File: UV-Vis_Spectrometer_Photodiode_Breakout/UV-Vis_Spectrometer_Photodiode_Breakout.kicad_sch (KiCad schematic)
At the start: 0 parts

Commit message: UV-Vis Photometer Circuit Diagram
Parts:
- added C1, C5, C6: C, symbol Device:C
- added C7, C9: 0.1uF, symbol Device:C
- added C8: 10uF, symbol Device:C
- added D1: BPW21R, OptoDevice:Kodenshi_LG206D, symbol Device:D_Photo
- added R1: R_US, Package_DIP:DIP-8_W7.62mm, symbol Device:R_US
- added R4: 1k, symbol Device:R_US
- added U1: TLV8811DBVR, Package_TO_SOT_SMD:SOT-353_SC-70-5, symbol Amplifier_Operational:TLV172IDCK
- added U3: LTC2451, Package_DFN_QFN:DFN-8-1EP_2x3mm_P0.5mm_EP0.61x2.2mm, symbol Analog_ADC:LTC2451xDDB
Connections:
- new net: C1.1, D1.1 (K), R1.1, U1.3 (-)
- new net: C1.2, R1.2, U1.4
- new net: C9.1, R4.2, U3.6 (IN)
- new net +3.3V: C7.1, C8.1, U3.3 (REF+), U3.4 (VCC)
- new net +3V3: C5.1, C6.1, U1.5 (V+)
- new net Clock: U3.7 (SCL)
- new net Data: U3.8 (SDA)
- new net GND: C5.2, C6.2, C7.2, C8.2, C9.2, D1.2 (A), U1.1 (+), U1.2 (V-), U3.1 (GND), U3.2 (REF-), U3.5 (GND), U3.9 (GND)
- new net Out_TIA: R4.1
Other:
- added sheet Power (untitled.kicad_sch)

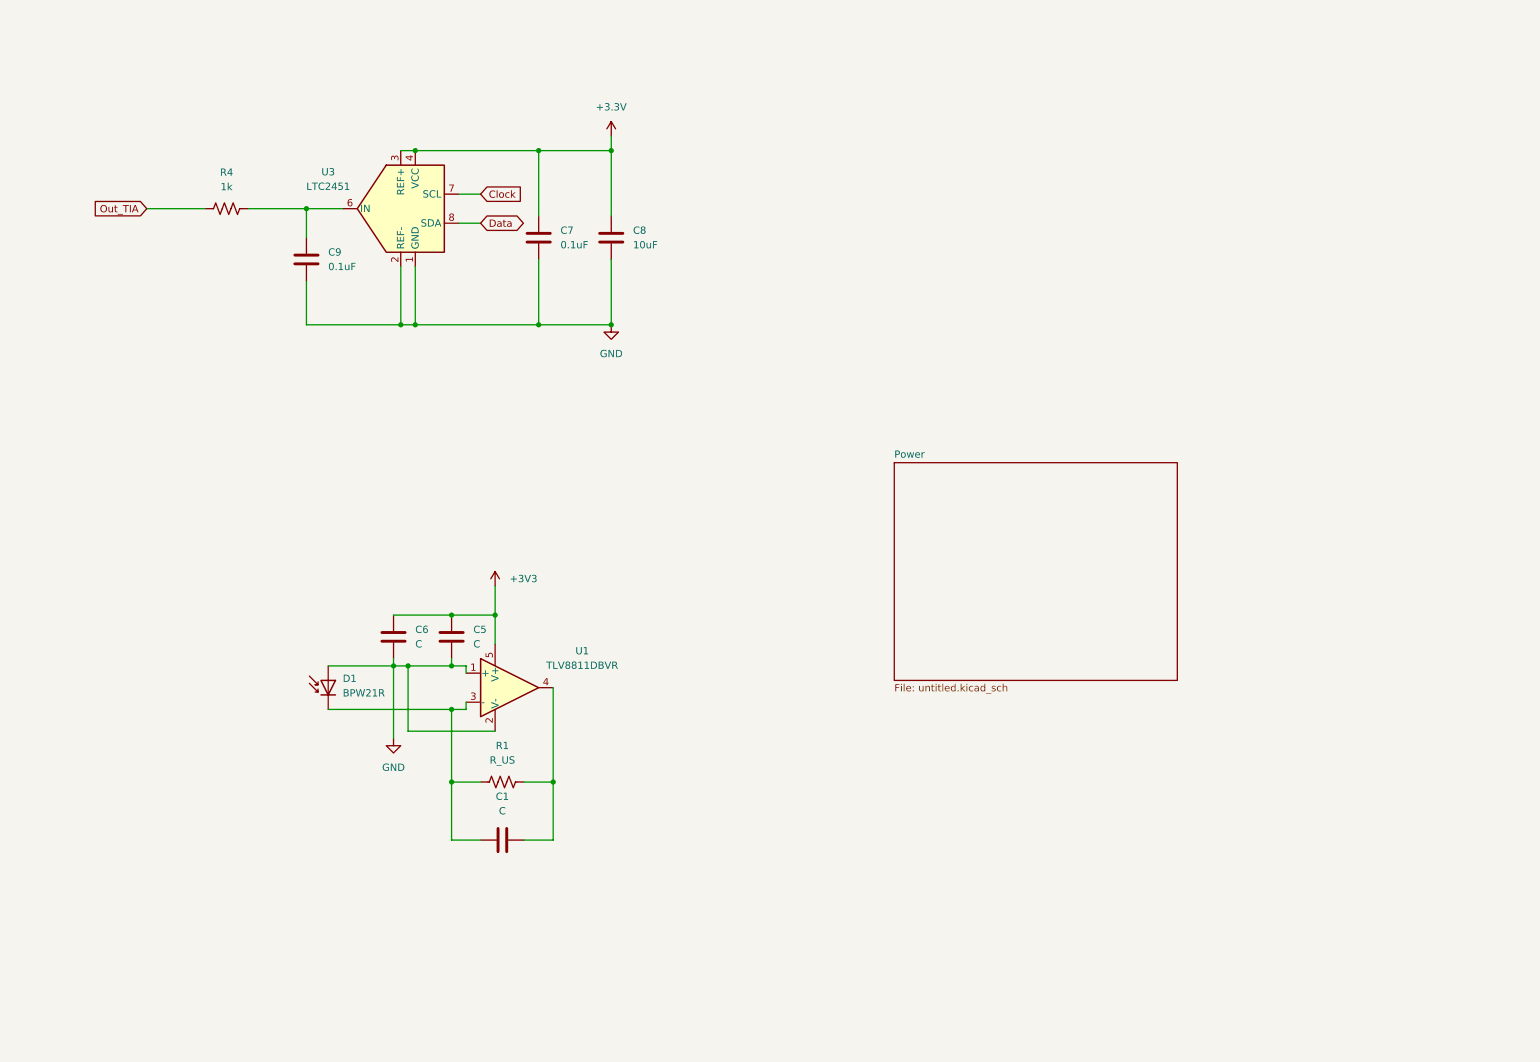
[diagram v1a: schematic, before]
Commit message: added reed switches, res values needed
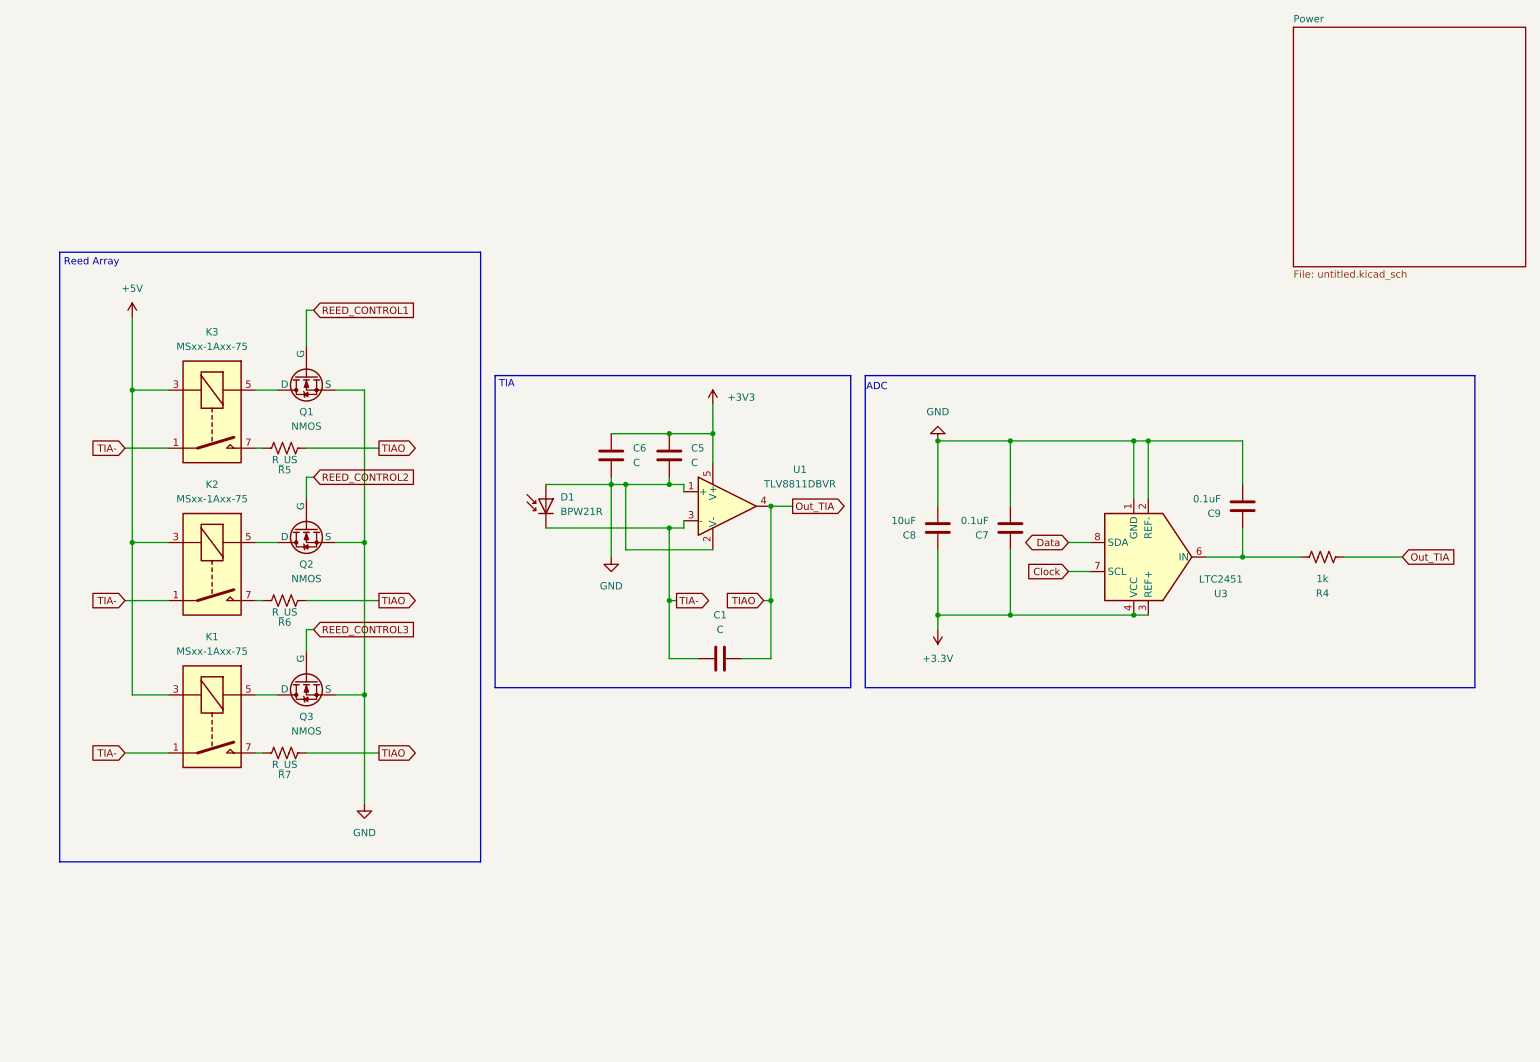
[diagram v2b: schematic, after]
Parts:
- removed R1: R_US, Package_DIP:DIP-8_W7.62mm, symbol Device:R_US
- added K1, K2, K3: MSxx-1Axx-75, Relay_THT:Relay_SPST_StandexMeder_MS_Form1AB, symbol Relay:MSxx-1Axx-75
- added Q1, Q2, Q3: NMOS, Package_DFN_QFN:Nordic_AQFN-94-1EP_7x7mm_P0.4mm, symbol Simulation_SPICE:NMOS
- added R5, R6, R7: R_US, Package_DIP:DIP-8_W7.62mm, symbol Device:R_US
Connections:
- net GND: now also Q1.3 (S), Q2.3 (S), Q3.3 (S)
- net Out_TIA: now also C1.2, U1.4, R5.2, R6.2, R7.2
- net TIA-: now reaches C1.1, D1.1 (K), U1.3 (-)
- net TIA-: now also K1.1, K2.1, K3.1
- new net: K2.7, R6.1
- new net: K3.5, Q1.1 (D)
- new net: K3.7, R5.1
- new net: K1.5, Q3.1 (D)
- new net: K2.5, Q2.1 (D)
- new net: K1.7, R7.1
- new net +5V: K1.3, K2.3, K3.3
- new net REED_CONTROL1: Q1.2 (G)
- new net REED_CONTROL2: Q2.2 (G)
- new net REED_CONTROL3: Q3.2 (G)
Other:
- note added: "ADC"
- note added: "Reed Array"
- note added: "TIA"
- moved on the sheet: C1, C5, C6, C7, C8, C9, D1, R4, U1, U3

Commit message: Added Connectors and Resistance values for the TIA
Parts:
- added J1: Conn_01x05, Package_DFN_QFN:QFN-20-1EP_5x5mm_P0.65mm_EP3.35x3.35mm, symbol Connector_Generic:Conn_01x05
- added J2: Conn_01x02, Package_DFN_QFN:QFN-20-1EP_5x5mm_P0.65mm_EP3.35x3.35mm, symbol Connector_Generic:Conn_01x02
- added J3: Conn_01x02, symbol Connector_Generic:Conn_01x02
- C1: value C -> 46pF
- C5: value C -> 10uF
- C6: value C -> 0.1uF
- R5: value R_US -> 5.1k
- R6: value R_US -> 8.2k
- R7: value R_US -> 16k
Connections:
- net +3V3: now also J3.1 (Pin_1)
- net +5V: now also J1.1 (Pin_1)
- net Clock: now also J2.2 (Pin_2)
- net Data: now also J2.1 (Pin_1)
- net GND: now also J1.2 (Pin_2), J3.2 (Pin_2)
- net REED_CONTROL1: now also J1.3 (Pin_3)
- net REED_CONTROL2: now also J1.4 (Pin_4)
- net REED_CONTROL3: now also J1.5 (Pin_5)

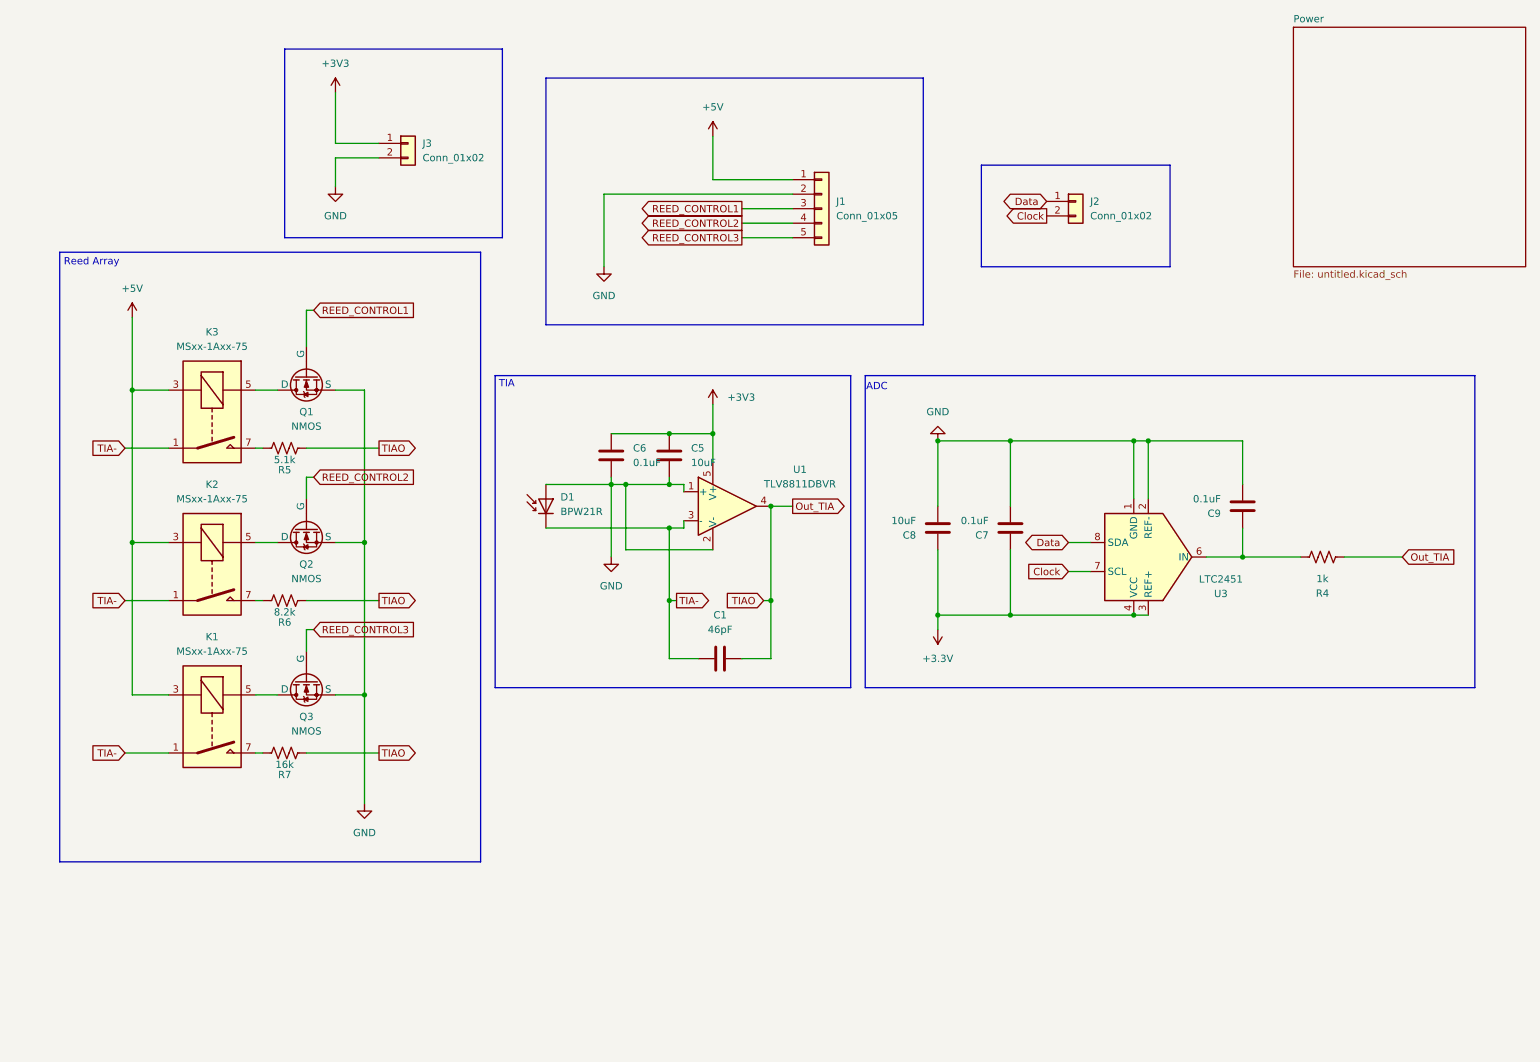
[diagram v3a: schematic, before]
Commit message: Cleaned up op amp circuit. Added Vref. Made reed relay symbol.
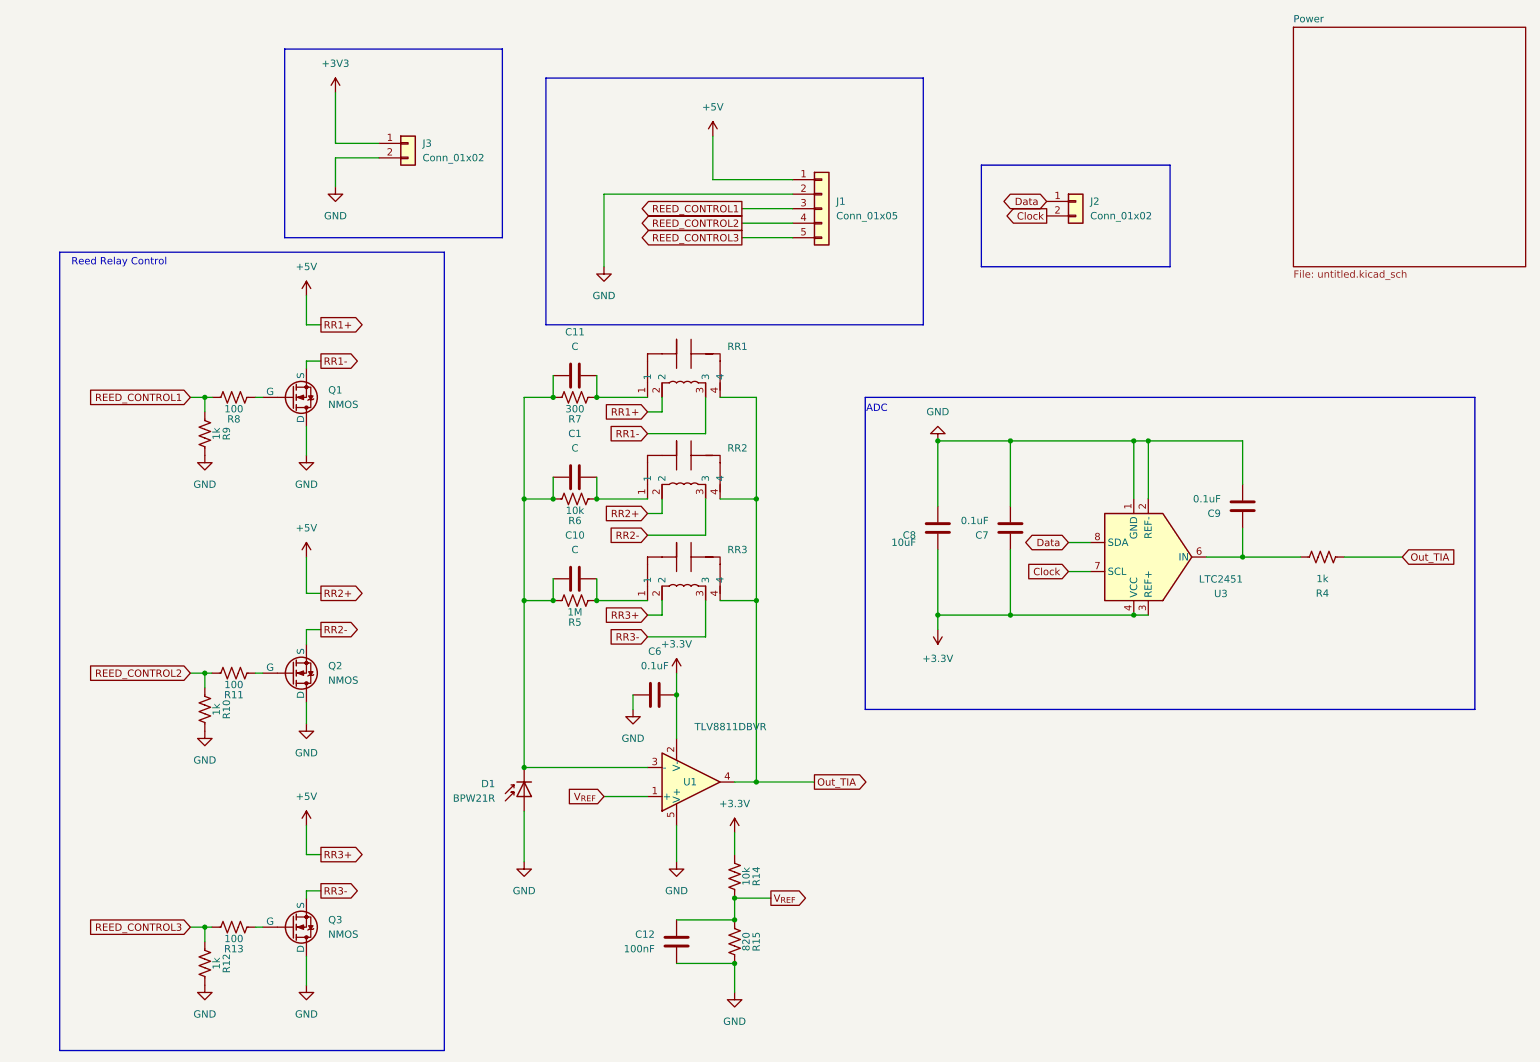
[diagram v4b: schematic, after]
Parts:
- removed C5: 10uF, symbol Device:C
- removed K1, K2, K3: MSxx-1Axx-75, Relay_THT:Relay_SPST_StandexMeder_MS_Form1AB, symbol Relay:MSxx-1Axx-75
- added C10, C11: C, symbol Device:C
- added C12: 100nF, symbol Device:C
- added R10, R12, R9: 1k, Package_DIP:DIP-8_W7.62mm, symbol Device:R_US
- added R11, R13, R8: 100, Package_DIP:DIP-8_W7.62mm, symbol Device:R_US
- added R14: 10k, Package_DIP:DIP-8_W7.62mm, symbol Device:R_US
- added R15: 820, Package_DIP:DIP-8_W7.62mm, symbol Device:R_US
- added RR1, RR2, RR3: (no value), symbol UV-Vis_Symbol_Library:9007-05-00
- C1: value 46pF -> C
- R5: value 5.1k -> 1M
- R6: value 8.2k -> 10k
- R7: value 16k -> 300
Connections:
- net TIA- is gone; now on an unnamed net: C1.1, D1.1 (K), U1.3 (-)
- net +3.3V: now also C6.2, U1.2 (V-), R14.2
- net +3V3: no longer C6.1, U1.5 (V+)
- net +5V: now also RR1.2, RR2.2, RR3.2
- net GND: now also C6.1, Q1.1 (D), Q2.1 (D), Q3.1 (D), U1.5 (V+), C12.2, R10.1, R12.1, R15.1, R9.1; no longer C6.2, Q1.3 (S), Q2.3 (S), Q3.3 (S), U1.1 (+), U1.2 (V-)
- net Out_TIA: now also RR1.4, RR2.4, RR3.4; no longer C1.2, R5.2, R6.2, R7.2
- net REED_CONTROL1: now also R8.1, R9.2; no longer Q1.2 (G)
- net REED_CONTROL2: now also R10.2, R11.1; no longer Q2.2 (G)
- net REED_CONTROL3: now also R12.2, R13.1; no longer Q3.2 (G)
- net at R6.1: now also R5.1, R7.1, C10.1, C11.1
- new net: C1.2, R6.2, RR2.1
- new net: Q3.2 (G), R13.2
- new net: Q2.2 (G), R11.2
- new net: Q1.2 (G), R8.2
- new net: C11.2, R7.2, RR1.1
- new net: C10.2, R5.2, RR3.1
- new net RR1-: Q1.3 (S), RR1.3
- new net RR2-: Q2.3 (S), RR2.3
- new net RR3-: Q3.3 (S), RR3.3
- new net V_{REF}: C12.1, R14.1, R15.2, U1.1 (+)
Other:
- note added: "Reed Relay Control"
- note removed: "Reed Array"
- note removed: "TIA"
- moved on the sheet: C1, C6, D1, Q1, Q2, Q3, R5, R6, R7, U1

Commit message: Made some nice boxes and labels.
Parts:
- added C2: 10uF, symbol Device:C
- added C3: .1uF, symbol Device:C
- added C4: 1uF, Package_SO:SOIC-8_3.9x4.9mm_P1.27mm, symbol Device:C_US
- added D2, D3: 1N4001, Diode_THT:D_DO-41_SOD81_P10.16mm_Horizontal, symbol Diode:1N4001
- added R2: 3.3k, Package_DIP:DIP-8_W7.62mm, symbol Device:R_US
- added R3: 2.2k, Package_DIP:DIP-8_W7.62mm, symbol Device:R_US
- added U2: LM317BS-TR, Package_SO:SOIC-8_3.9x4.9mm_P1.27mm, symbol Regulator_Linear:LM317L_SO8
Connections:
- net +3V3: now also C4.1, D2.2 (A), D3.1 (K), R2.1, U2.2 (VO), U2.3 (VO), U2.6 (VO), U2.7 (VO)
- net +5V: now also C3.1, D2.1 (K), U2.1 (VI)
- net GND: now also C2.2, C3.2, C4.2, R3.2
- new net: C2.1, D3.2 (A), R2.2, R3.1, U2.4 (ADJ)
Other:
- removed sheet Power
- note added: "Power"
- note added: "TIA"
- moved on the sheet: C7, C8, C9, J1, J2, J3, Q1, Q2, Q3, R10, R11, R12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

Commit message: Added footprints and started layouts.
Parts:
- removed C4: 1uF, Package_SO:SOIC-8_3.9x4.9mm_P1.27mm, symbol Device:C_US
- removed Q1, Q2, Q3: NMOS, Package_DFN_QFN:Nordic_AQFN-94-1EP_7x7mm_P0.4mm, symbol Simulation_SPICE:NMOS
- added C4: 1uF, Capacitor_SMD:C_0603_1608Metric_Pad1.08x0.95mm_HandSolder, symbol Device:C
- added D4: Green, LED_SMD:LED_Cree-XHP50_3V_HighDensity, symbol Device:LED
- added D5: Green, Diode_SMD:D_0603_1608Metric_Pad1.05x0.95mm_HandSolder, symbol Device:LED
- added Q1, Q2, Q3: BSS138BK,215, Package_TO_SOT_SMD:SOT-23, symbol Transistor_FET:BSS138
- added R16: 820, Resistor_SMD:R_0603_1608Metric_Pad0.98x0.95mm_HandSolder, symbol Device:R_US
- added R17: 330, Resistor_SMD:R_0603_1608Metric_Pad0.98x0.95mm_HandSolder, symbol Device:R_US
- added U4, U5, U6, U7: (no value), MRDT_Drill_Holes:4_40_Hole_Pad_Via, symbol MRDT_Connectors:4_40_Mounting_Hole_Pad
- C1, C10, C11, C2, C6, C7, C8, C9: footprint (none) -> Capacitor_SMD:C_0603_1608Metric_Pad1.08x0.95mm_HandSolder
- C12: value 100nF -> 0.1uF; footprint (none) -> Capacitor_SMD:C_0603_1608Metric_Pad1.08x0.95mm_HandSolder
- C3: value .1uF -> 0.1uF; footprint (none) -> Capacitor_SMD:C_0603_1608Metric_Pad1.08x0.95mm_HandSolder
- J1: footprint Package_DFN_QFN:QFN-20-1EP_5x5mm_P0.65mm_EP3.35x3.35mm -> Connector_JST:JST_PH_S5B-PH-K_1x05_P2.00mm_Horizontal
- J2: footprint Package_DFN_QFN:QFN-20-1EP_5x5mm_P0.65mm_EP3.35x3.35mm -> Connector_JST:JST_PH_S2B-PH-K_1x02_P2.00mm_Horizontal
- J3: footprint (none) -> Connector_JST:JST_PH_S2B-PH-K_1x02_P2.00mm_Horizontal
- R10, R12, R9: value 1k -> 10k; footprint Package_DIP:DIP-8_W7.62mm -> Resistor_SMD:R_0603_1608Metric_Pad0.98x0.95mm_HandSolder
- R11, R13, R14, R15, R2, R3, R8: footprint Package_DIP:DIP-8_W7.62mm -> Resistor_SMD:R_0603_1608Metric_Pad0.98x0.95mm_HandSolder
- R4: footprint (none) -> Resistor_SMD:R_0603_1608Metric_Pad0.98x0.95mm_HandSolder
- R5: value 1M -> R; footprint Package_DIP:DIP-8_W7.62mm -> Resistor_SMD:R_0603_1608Metric_Pad0.98x0.95mm_HandSolder
- R6: value 10k -> R; footprint Package_DIP:DIP-8_W7.62mm -> Resistor_SMD:R_0603_1608Metric_Pad0.98x0.95mm_HandSolder
- R7: value 300 -> R; footprint Package_DIP:DIP-8_W7.62mm -> Resistor_SMD:R_0603_1608Metric_Pad0.98x0.95mm_HandSolder
- RR1, RR2, RR3: footprint (none) -> Relay_THT:Relay_SPST_StandexMeder_SIL_Form1A
- U1: footprint Package_TO_SOT_SMD:SOT-353_SC-70-5 -> Package_TO_SOT_SMD:SOT-23-5_HandSoldering
- U3: footprint Package_DFN_QFN:DFN-8-1EP_2x3mm_P0.5mm_EP0.61x2.2mm -> Package_TO_SOT_SMD:TSOT-23-8_HandSoldering
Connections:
- net +3.3V: now also U1.5 (V+); no longer C7.1, C8.1, R14.2, U1.2 (V-), U3.3 (REF+), U3.4 (VCC)
- net +3V3: now also C7.1, C8.1, R14.2, U3.3 (REF+), U3.4 (VCC), C4.1, D4.2 (A)
- net +5V: now also D5.2 (A)
- net GND: now also U1.2 (V-), C4.2, Q1.2 (S), Q2.2 (S), Q3.2 (S), R16.2, R17.2, U4.1, U5.1, U6.1, U7.1; no longer U1.5 (V+)
- net RR1-: now also Q1.3 (D)
- net RR2-: now also Q2.3 (D)
- net RR3-: now also Q3.3 (D)
- net at R13.2: now also Q3.1 (G)
- net at R11.2: now also Q2.1 (G)
- net at R8.2: now also Q1.1 (G)
- new net: D4.1 (K), R17.1
- new net: D5.1 (K), R16.1
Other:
- note added: "3V power"
- note added: "I2C Connector"
- note added: "Reed Relay Control Connector"
